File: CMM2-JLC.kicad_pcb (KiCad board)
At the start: 4 copper layers, 130 x 102 mm, 3 parts, among them J1 Nunchuck, U1 STM32H743IITx, U2 MT48LC16M16A2P

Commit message: first component routing
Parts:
- added BT1: CR2032, CMM2-JLC:BatteryHolder_CR2032-BS-6-1, F.Cu at (38.4, 86.8)
- added C1: 100n, Capacitor_SMD:C_0402_1005Metric, F.Cu at (254.1, 65.7)
- added C10: 6p, Capacitor_SMD:C_0402_1005Metric, F.Cu at (233.7, 84.8)
- added C11: 20p, Capacitor_SMD:C_0402_1005Metric, F.Cu at (290.1, 28.6)
- added C12: 20p, Capacitor_SMD:C_0402_1005Metric, F.Cu at (251.2, 63.7)
- added C13: 1u, Capacitor_SMD:C_0402_1005Metric, F.Cu at (254.1, 63.7)
- added C14: 100n, Capacitor_SMD:C_0402_1005Metric, F.Cu at (267.9, 51.5)
- added C15: 4.7u, Capacitor_SMD:C_0402_1005Metric, F.Cu at (233.7, 82.9)
- added C16: 100n, Capacitor_SMD:C_0402_1005Metric, F.Cu at (285.0, 33.6)
- added C17: 10u, Capacitor_SMD:C_0603_1608Metric, F.Cu at (35.3, 42.5)
- added C18: 100n, Capacitor_SMD:C_0402_1005Metric, F.Cu at (33.8, 42.4)
- added C19: 1u, Capacitor_SMD:C_0402_1005Metric, F.Cu at (258.1, 60.5)
- added C2: 100n, Capacitor_SMD:C_0402_1005Metric, F.Cu at (236.7, 82.3)
- added C20: 100n, Capacitor_SMD:C_0402_1005Metric, F.Cu at (46.4, 42.5)
- added C21: 22u, Capacitor_SMD:C_0603_1608Metric, F.Cu at (44.9, 42.6)
- added C22: 100n, Capacitor_SMD:C_0402_1005Metric, F.Cu at (259.8, 56.5)
- added C23: 100n, Capacitor_SMD:C_0402_1005Metric, F.Cu at (272.2, 46.5)
- added C3: 100n, Capacitor_SMD:C_0402_1005Metric, F.Cu at (276.2, 43.5)
- added C4: 100n, Capacitor_SMD:C_0402_1005Metric, F.Cu at (246.8, 70.1)
- added C5: 100n, Capacitor_SMD:C_0402_1005Metric, F.Cu at (226.5, 91.6)
- added C6: 2.2u, Capacitor_SMD:C_0603_1608Metric, F.Cu at (235.3, 70.6)
- added C7: 2.2u, Capacitor_SMD:C_0603_1608Metric, F.Cu at (257.5, 51.7)
- added C8: 1u, Capacitor_SMD:C_0402_1005Metric, F.Cu at (245.7, 72.6)
- added C9: 6p, Capacitor_SMD:C_0402_1005Metric, F.Cu at (264.9, 53.4)
- added D1: SD CARD / RED, LED_SMD:LED_0603_1608Metric, F.Cu at (231.3, 73.0)
- added D2: POWER / GREEN, LED_SMD:LED_0603_1608Metric, F.Cu at (229.6, 70.4)
- added J2: VGA, Connector_Dsub:DSUB-15-HD_Male_Horizontal_P2.29x1.98mm_EdgePinOffset8.35mm_Housed_MountingHolesOffset10.89mm, F.Cu at (137.5, 39.9)
- added J3: EXTERNAL I/O, Connector_IDC:IDC-Header_2x20_P2.54mm_Vertical, F.Cu at (63.0, 26.9)
- added J4: USB_C_Receptacle_USB2.0, Connector_USB:USB_C_Receptacle_Palconn_UTC16-G, F.Cu at (42.9, 24.4)
- added J5: Audio, CMM2-JLC:PJ-3270, F.Cu at (52.6, 22.4)
- added J6: USB A Host, Connector_USB:USB_A_Molex_67643_Horizontal, F.Cu at (32.5, 33.5)
- added J7: SWD, Connector_PinHeader_2.54mm:PinHeader_1x05_P2.54mm_Vertical, F.Cu at (109.1, 60.3)
- added J8: Micro_SD_Card_Det, CMM2-JLC:HOAUC_HYC77-TF09-200, F.Cu at (81.5, 116.2)
- added J9: Boot select, Connector_PinHeader_2.54mm:PinHeader_1x03_P2.54mm_Vertical, F.Cu at (108.3, 88.8)
- added R1: 10k, Resistor_SMD:R_0402_1005Metric, F.Cu at (251.2, 65.7)
- added R10: 240R, Resistor_SMD:R_0603_1608Metric, F.Cu at (237.7, 67.8)
- added R11: 240R, Resistor_SMD:R_0603_1608Metric, F.Cu at (231.3, 78.1)
- added R12: 240R, Resistor_SMD:R_0603_1608Metric, F.Cu at (247.7, 61.7)
- added R13: 120R, Resistor_SMD:R_0603_1608Metric, F.Cu at (250.2, 59.0)
- added R14: 120R, Resistor_SMD:R_0603_1608Metric, F.Cu at (235.3, 73.1)
- added R15: 120R, Resistor_SMD:R_0603_1608Metric, F.Cu at (226.3, 84.3)
- added R16: 240R, Resistor_SMD:R_0603_1608Metric, F.Cu at (227.0, 89.4)
- added R17: 240R, Resistor_SMD:R_0603_1608Metric, F.Cu at (272.8, 44.3)
- added R18: 240R, Resistor_SMD:R_0603_1608Metric, F.Cu at (261.5, 54.2)
- added R19: 120R, Resistor_SMD:R_0603_1608Metric, F.Cu at (228.8, 81.8)
- added R2: 10k, Resistor_SMD:R_0402_1005Metric, F.Cu at (282.1, 35.6)
- added R20: 120R, Resistor_SMD:R_0603_1608Metric, F.Cu at (272.8, 41.8)
- added R21: 120R, Resistor_SMD:R_0603_1608Metric, F.Cu at (251.7, 61.5)
- added R22: 240R, Resistor_SMD:R_0603_1608Metric, F.Cu at (223.0, 88.3)
- added R23: 240R, Resistor_SMD:R_0603_1608Metric, F.Cu at (243.4, 70.3)
- added R24: 240R, Resistor_SMD:R_0603_1608Metric, F.Cu at (239.4, 72.8)
- added R25: 120R, Resistor_SMD:R_0603_1608Metric, F.Cu at (235.3, 78.1)
- added R26: 120R, Resistor_SMD:R_0603_1608Metric, F.Cu at (245.7, 67.8)
- added R27: 120R, Resistor_SMD:R_0603_1608Metric, F.Cu at (231.3, 75.6)
- added R28: 240R, Resistor_SMD:R_0603_1608Metric, F.Cu at (223.0, 90.8)
- added R29: 240R, Resistor_SMD:R_0603_1608Metric, F.Cu at (219.0, 90.6)
- added R3: 10k, Resistor_SMD:R_0402_1005Metric, F.Cu at (249.7, 67.7)
- added R30: 240R, Resistor_SMD:R_0603_1608Metric, F.Cu at (247.7, 64.2)
- added R31: 120R, Resistor_SMD:R_0603_1608Metric, F.Cu at (254.2, 59.0)
- added R32: 120R, Resistor_SMD:R_0603_1608Metric, F.Cu at (261.5, 51.7)
- added R33: 120R, Resistor_SMD:R_0603_1608Metric, F.Cu at (257.5, 54.2)
- added R34: 240R, Resistor_SMD:R_0603_1608Metric, F.Cu at (277.6, 37.1)
- added R35: 75R, Resistor_SMD:R_0603_1608Metric, F.Cu at (239.4, 75.3)
- added R36: 240R, Resistor_SMD:R_0603_1608Metric, F.Cu at (230.3, 84.3)
- added R37: 240R, Resistor_SMD:R_0603_1608Metric, F.Cu at (232.8, 80.6)
- added R38: 75R, Resistor_SMD:R_0603_1608Metric, F.Cu at (286.6, 28.9)
- added R39: 120R, Resistor_SMD:R_0603_1608Metric, F.Cu at (227.0, 86.9)
- added R4: 10k, Resistor_SMD:R_0402_1005Metric, F.Cu at (276.2, 41.5)
- added R40: 240R, Resistor_SMD:R_0603_1608Metric, F.Cu at (282.6, 31.4)
- added R41: 75R, Resistor_SMD:R_0603_1608Metric, F.Cu at (239.4, 70.3)
- added R42: 10k, Resistor_SMD:R_0402_1005Metric, F.Cu at (242.8, 74.6)
- added R43: 10R, Resistor_SMD:R_0402_1005Metric, F.Cu at (256.9, 56.5)
- added R44: 5.1k, Resistor_SMD:R_0402_1005Metric, F.Cu at (230.5, 86.6)
- added R45: 5.1k, Resistor_SMD:R_0402_1005Metric, F.Cu at (286.1, 31.1)
- added R46: 4.7k, Resistor_SMD:R_0402_1005Metric, F.Cu at (236.3, 80.3)
- added R47: 3.3k, Resistor_SMD:R_0402_1005Metric, F.Cu at (238.8, 77.6)
- added R48: 4.7k, Resistor_SMD:R_0402_1005Metric, F.Cu at (277.1, 39.4)
- added R49: 4.7k, Resistor_SMD:R_0402_1005Metric, F.Cu at (264.9, 51.5)
- added R5: 10k, Resistor_SMD:R_0402_1005Metric, F.Cu at (242.8, 72.6)
- added R50: 120R, Resistor_SMD:R_0603_1608Metric, F.Cu at (215.0, 90.6)
- added R51: 100k, Resistor_SMD:R_0402_1005Metric, F.Cu at (129.1, -12.9)
- added R52: 10k, Resistor_SMD:R_0402_1005Metric, F.Cu at (257.7, 58.5)
- added R6: 10k, Resistor_SMD:R_0402_1005Metric, F.Cu at (274.9, 23.3)
- added R7: 240R, Resistor_SMD:R_0603_1608Metric, F.Cu at (235.3, 75.6)
- added R8: 240R, Resistor_SMD:R_0603_1608Metric, F.Cu at (241.7, 67.8)
- added R9: 240R, Resistor_SMD:R_0603_1608Metric, F.Cu at (282.6, 28.9)
- added SW1: Reset, CMM2-JLC:TS-1187A-X-X-X, F.Cu at (126.4, -6.30)
- added TP-3V3: TestPoint, TestPoint:TestPoint_Pad_2.0x2.0mm, F.Cu at (201.0, 112.9)
- added TP-5V1: TestPoint, TestPoint:TestPoint_Pad_2.0x2.0mm, F.Cu at (191.3, 112.7)
- added TP-GND1: TestPoint, TestPoint:TestPoint_Pad_2.0x2.0mm, F.Cu at (210.6, 112.7)
- added U3: SRV05-4, Package_TO_SOT_SMD:SOT-23-6, F.Cu at (38.5, 34.6)
- added U4: CP2102N-A01-GQFN28, Package_DFN_QFN:QFN-28-1EP_5x5mm_P0.5mm_EP3.35x3.35mm, F.Cu at (50.6, 63.1)
- added U5: DS18B20, Package_TO_SOT_THT:TO-92_Inline, F.Cu at (25.9, 107.8)
- added U6: AMS1117-3.3, Package_TO_SOT_SMD:SOT-223-3_TabPin2, F.Cu at (40.1, 45.5)
- added U7: TSOP4838, OptoDevice:Vishay_MOLD-3Pin, F.Cu at (24.6, 115.6)
- added Y1: 32.768 kHz, Crystal:Crystal_SMD_3215-2Pin_3.2x1.5mm, F.Cu at (168.6, 115.0)
- added Y2: 8 MHz, Crystal:Crystal_SMD_5032-2Pin_5.0x3.2mm, F.Cu at (168.1, 101.0)
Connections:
- U1 pad 122: /PA11 -> /USB_HOST_D-
- U1 pad 123: /PA12 -> /USB_HOST_D+
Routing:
- net GND: track 0.00 -> 88.7 mm, vias 0 -> 61
- net +3V3: track 0.00 -> 51.6 mm, vias 0 -> 36
- net /PE9: track 7.01 -> 30.0 mm, vias 2 -> 0
- net /PE8: track 7.28 -> 28.3 mm
- net /PF11: track 10.5 -> 29.8 mm
- net /PE10: track 13.0 -> 31.9 mm, vias 2 -> 0
- net +5V: track 0.00 -> 17.2 mm, vias 0 -> 8
- net /USB_C_D-: track 0.00 -> 14.5 mm
- net /USB_C_D+: track 0.00 -> 13.2 mm
- net /USB_HOST_D+: track 0.00 -> 11.1 mm
- net /PE7: track 15.6 -> 26.1 mm, vias 2 -> 0
- net /USB_HOST_D-: track 0.00 -> 10.5 mm
- net /PG8: track 45.1 -> 38.1 mm, vias 2 -> 6
- net /PH6: track 22.3 -> 27.1 mm
- net /PG0: track 24.2 -> 26.9 mm
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- added copper zone on POWER, net +5V
- added copper zone on F.Cu, net GND
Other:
- rule trace_min: 0.127 -> 0.09

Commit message: before SDRAM re-route
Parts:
- moved U4 12.3 mm to (40.1, 56.7)
- moved J2 7.20 mm to (137.7, 32.7)
- moved J8 0.81 mm to (81.6, 117.0)

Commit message: before SDRAM re-route
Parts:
- moved J9 16.6 mm to (124.9, 87.7)
- moved U2 2.30 mm to (86.0, 94.3)
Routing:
- net /PD9: track 33.8 -> 0.00 mm
- net /PD8: track 32.9 -> 0.00 mm
- net /PD10: track 34.0 -> 1.40 mm
- net /PD14: track 37.6 -> 13.1 mm, vias 4 -> 2
- net /PE10: track 31.9 -> 18.1 mm
- net /PE7: track 26.1 -> 12.4 mm
- net /PE8: track 28.3 -> 14.8 mm
- net /PE9: track 30.0 -> 16.5 mm
- net GND: track 88.7 -> 82.6 mm, vias 61 -> 55
- net +3V3: track 51.6 -> 46.5 mm, vias 36 -> 31
- net /PE1: track 45.9 -> 48.6 mm
- net /PF5: track 34.7 -> 37.1 mm
- net /PG8: track 38.1 -> 40.4 mm
- net /PF4: track 34.4 -> 36.7 mm
- net /PG15: track 32.4 -> 34.7 mm
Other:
- net class SDRAM added: clearance 0.304, trace_width 0.289, via_dia 0.45, via_drill 0.2

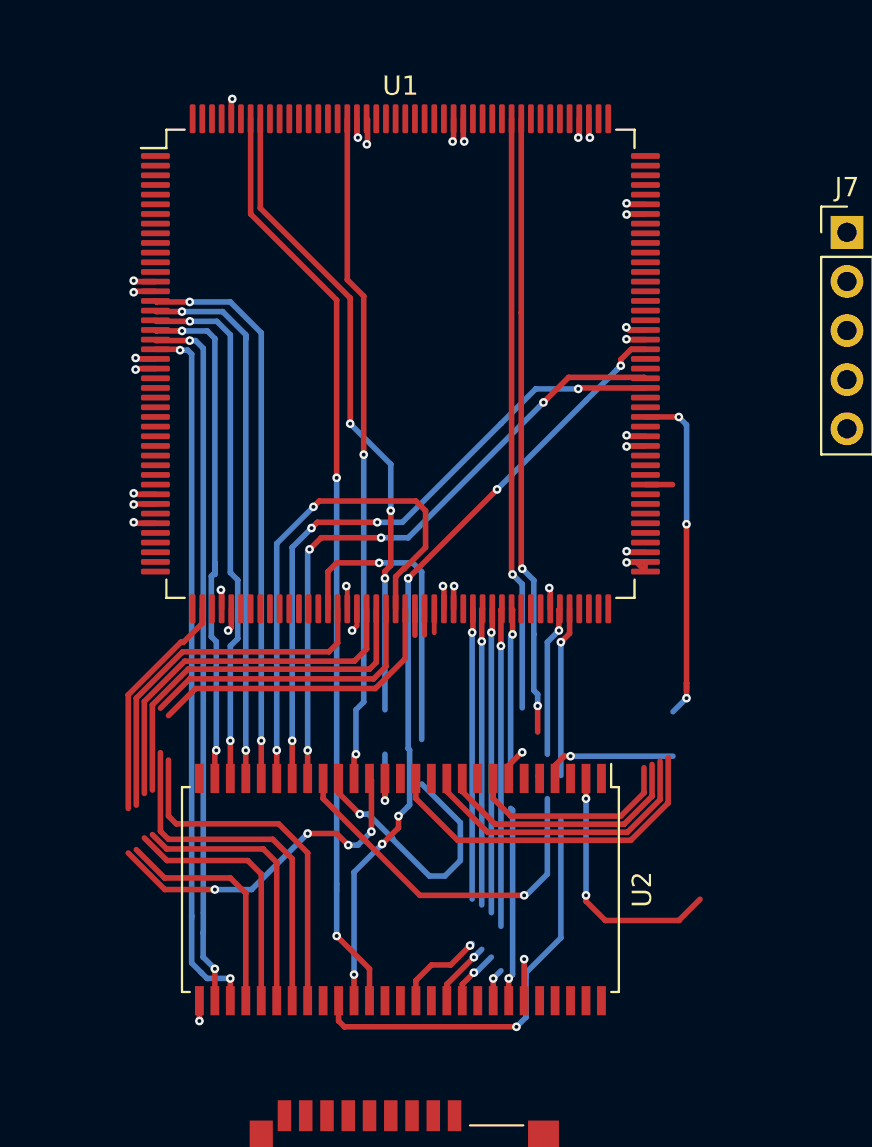
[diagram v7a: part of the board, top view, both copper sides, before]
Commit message: Layout SDRAM
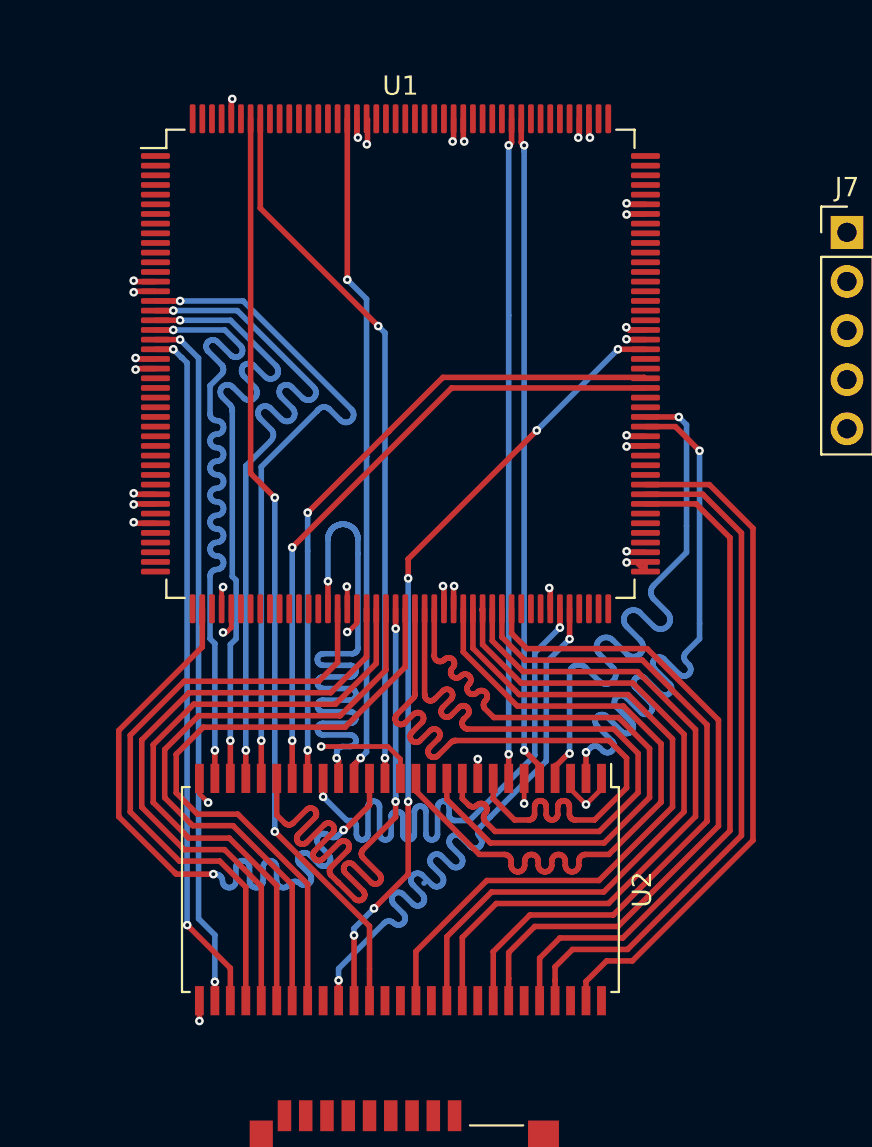
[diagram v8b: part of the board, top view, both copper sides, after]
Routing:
- net /PD9: track 0.00 -> 35.7 mm
- net /PD8: track 0.00 -> 35.0 mm
- net /PD10: track 1.40 -> 35.3 mm
- net /PE7: track 12.4 -> 37.5 mm
- net /PD14: track 13.1 -> 35.9 mm
- net /PE8: track 14.8 -> 34.4 mm
- net /PE10: track 18.1 -> 36.9 mm
- net /PE13: track 18.7 -> 36.5 mm, vias 2 -> 0
- net /PE12: track 18.7 -> 36.5 mm, vias 2 -> 0
- net /PE9: track 16.5 -> 33.9 mm
- net /PE15: track 18.2 -> 35.4 mm, vias 2 -> 0
- net /PE14: track 18.2 -> 35.3 mm, vias 2 -> 0
- net /PE11: track 19.8 -> 36.8 mm, vias 2 -> 0
- net /PG0: track 26.7 -> 37.3 mm
- net /PH5: track 29.9 -> 39.5 mm, vias 4 -> 2
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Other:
- net class SDRAM: clearance 0.304 -> 0.127
